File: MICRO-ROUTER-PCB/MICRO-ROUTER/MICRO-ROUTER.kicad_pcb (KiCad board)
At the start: 2 copper layers, 85 x 54 mm, 75 parts, among them J2 USB_A, J3 USB_C_Receptacle_USB2.0_16P, J4 Battery Connector, J5 SPI Header, J6 GPIO Header, J7 RJ45 5-2301996-6, Q1 FS8205A, SW2 8Devices Reset, SW3 UART Reset, U1 TP4056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

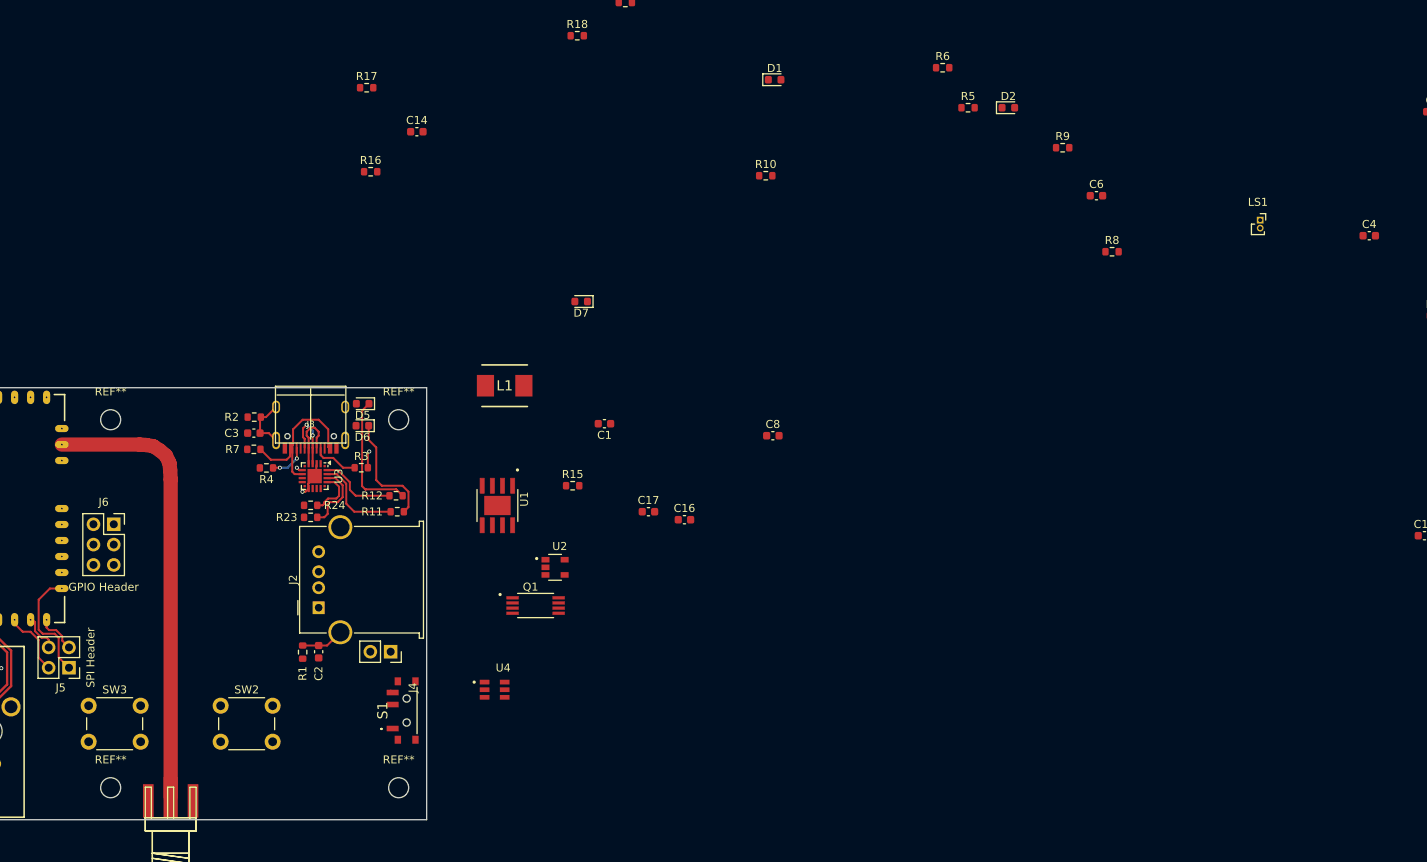
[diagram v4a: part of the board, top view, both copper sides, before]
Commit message: -added extra charge LED -wired TP4056
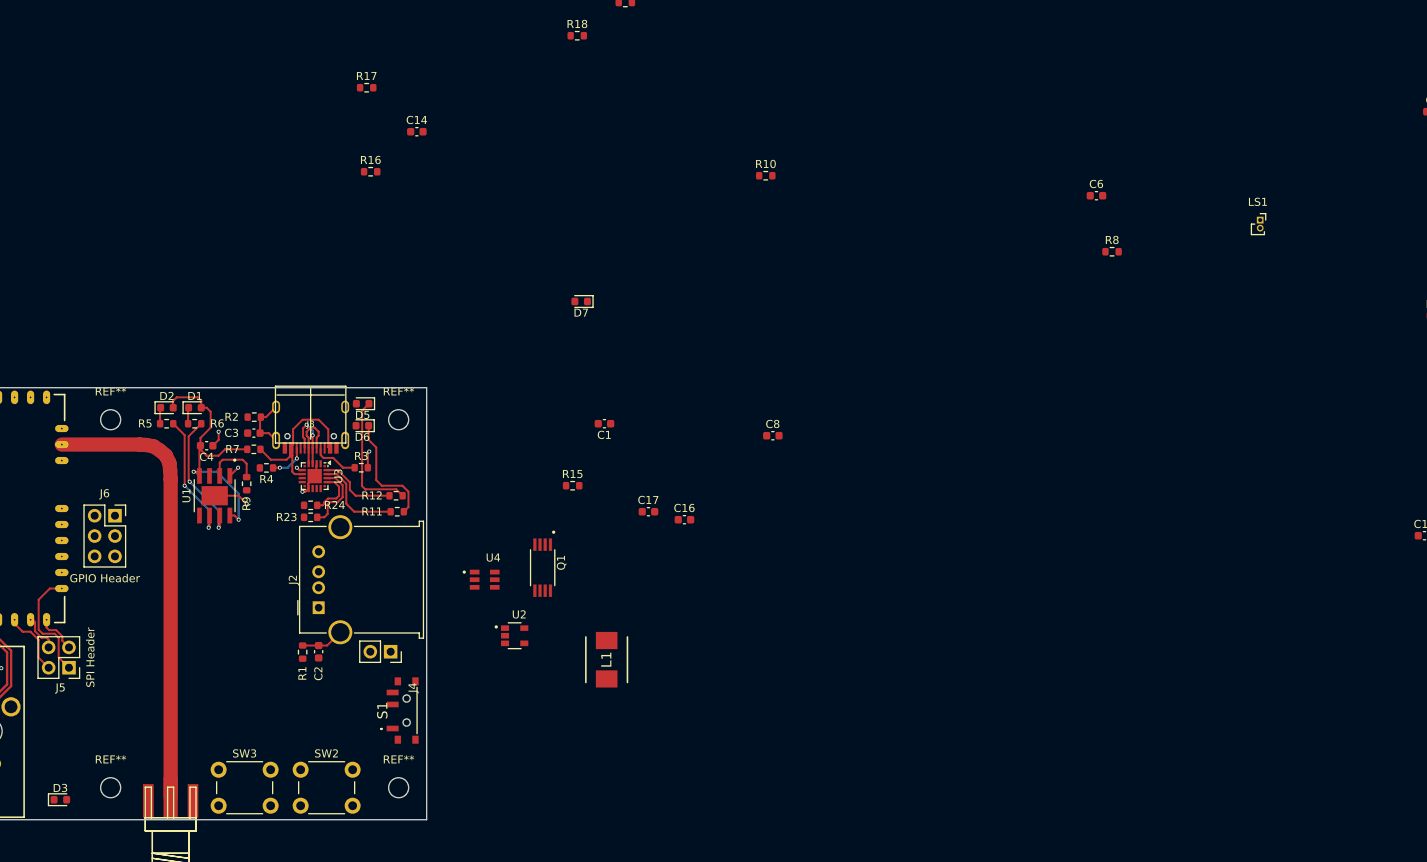
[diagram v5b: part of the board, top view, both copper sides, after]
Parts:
- added D3: LED Green, LED_SMD:LED_0603_1608Metric, F.Cu at (89.7, 184.5)
- moved C4 147.7 mm to (108.0, 140.2), turned to 180 degrees
- moved D2 111.7 mm to (103.0, 135.5)
- moved R9 110.3 mm to (113.0, 145.0), turned to -90 degrees
- moved R5 107.7 mm to (103.0, 137.5)
- moved R6 103.5 mm to (106.5, 137.5), turned to 180 degrees
- moved D1 83.3 mm to (106.5, 135.5)
- moved L1 36.5 mm to (158.0, 167.0), turned to 90 degrees
- moved U1 35.4 mm to (109.0, 146.5)
- moved SW3 18.1 mm to (109.5, 180.8)
- moved U4 13.8 mm to (142.8, 157.0)
- moved SW2 12.8 mm to (119.8, 180.8)
- moved U2 9.93 mm to (146.5, 164.0)
- moved Q1 4.81 mm to (150.0, 155.5), turned to -90 degrees
- moved J6 1.08 mm to (96.5, 149.0)
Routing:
- net Net-(D1-A): track 0.00 -> 34.9 mm, vias 0 -> 2
- net Net-(U1-~{CHRG}): track 0.00 -> 16.8 mm, vias 0 -> 2
- net Net-(U1-~{STDBY}): track 0.00 -> 16.4 mm, vias 0 -> 2
- net GND: track 6.55 -> 14.5 mm, vias 2 -> 5
- net Net-(U1-PROG): track 0.00 -> 7.06 mm
- net Net-(D2-K): track 0.00 -> 2.03 mm
- net Net-(D1-K): track 0.00 -> 2.03 mm
- net VBUS: track 20.1 -> 21.2 mm

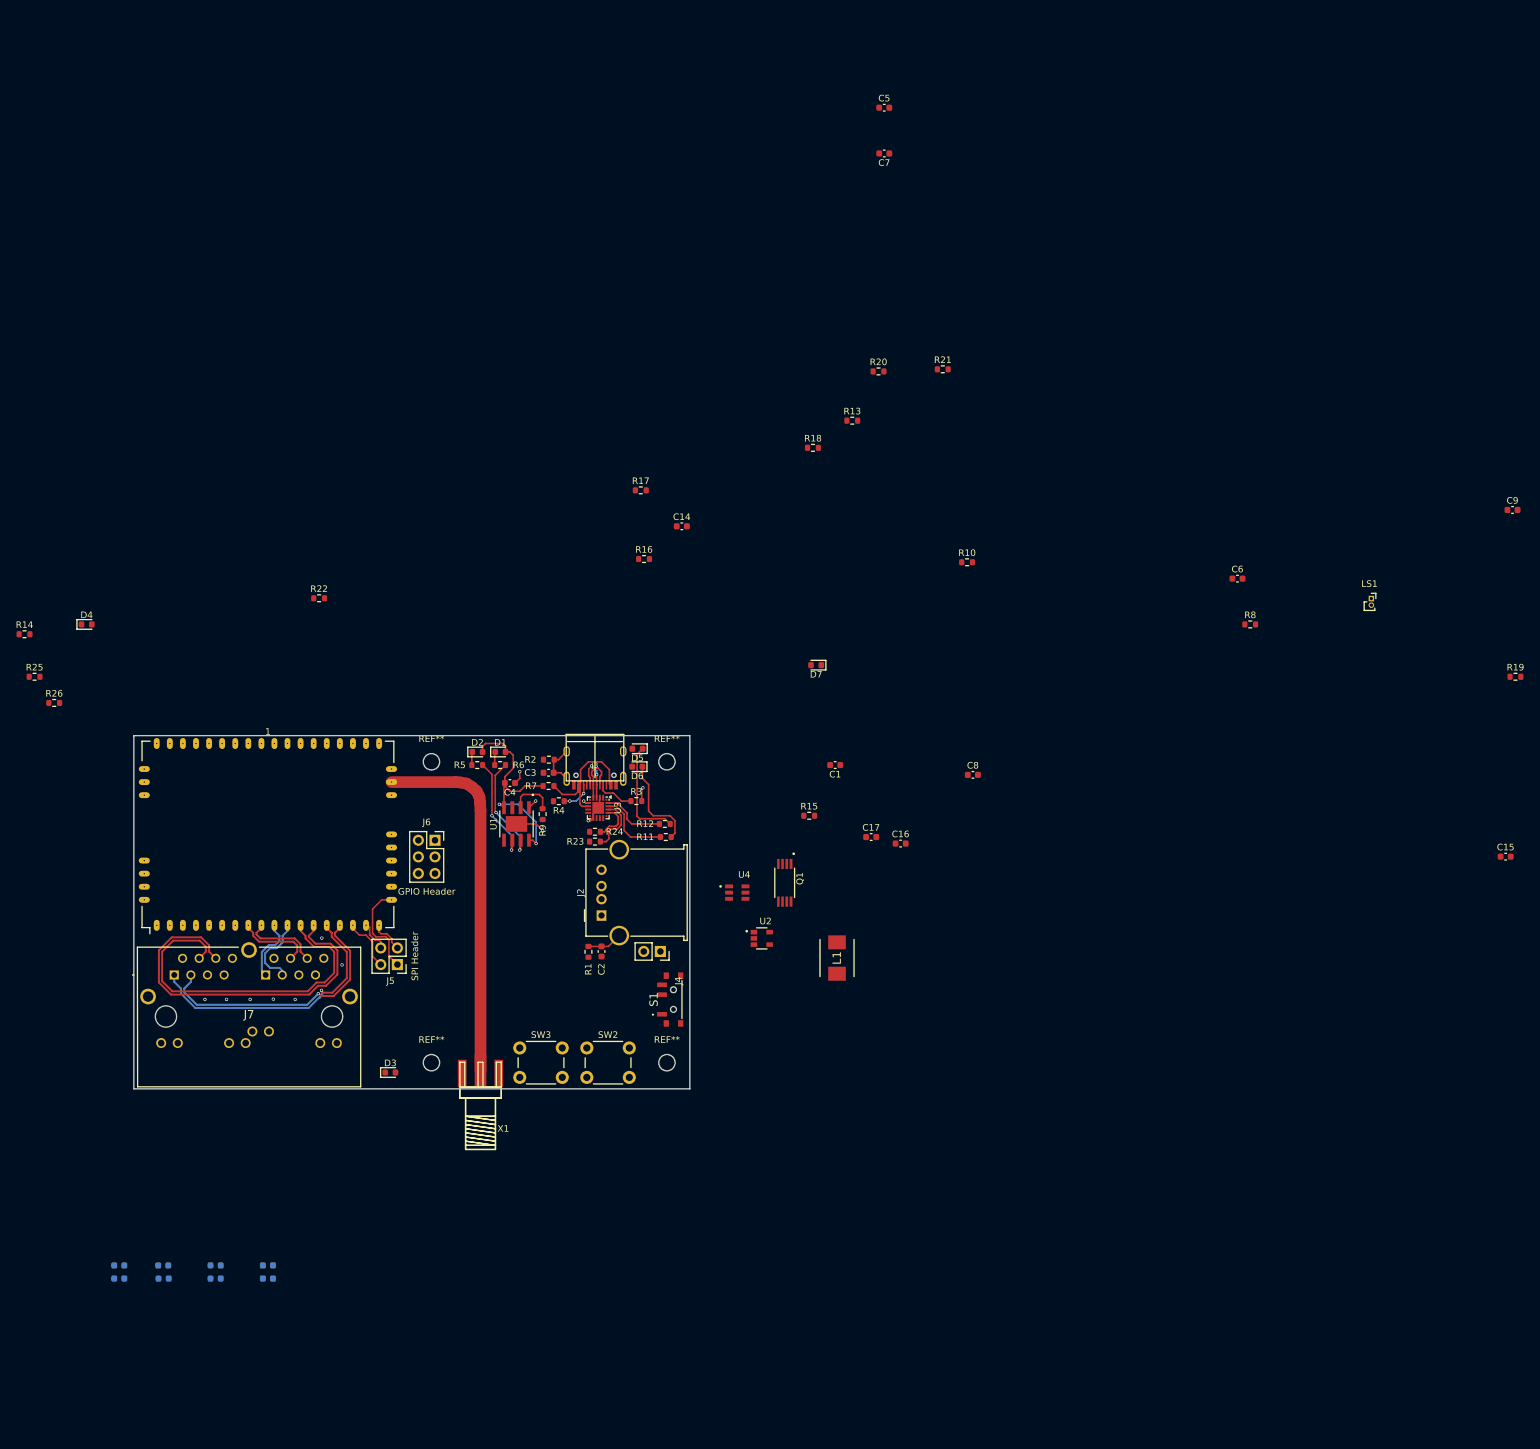
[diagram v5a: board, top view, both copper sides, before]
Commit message: -Wired up Mofset
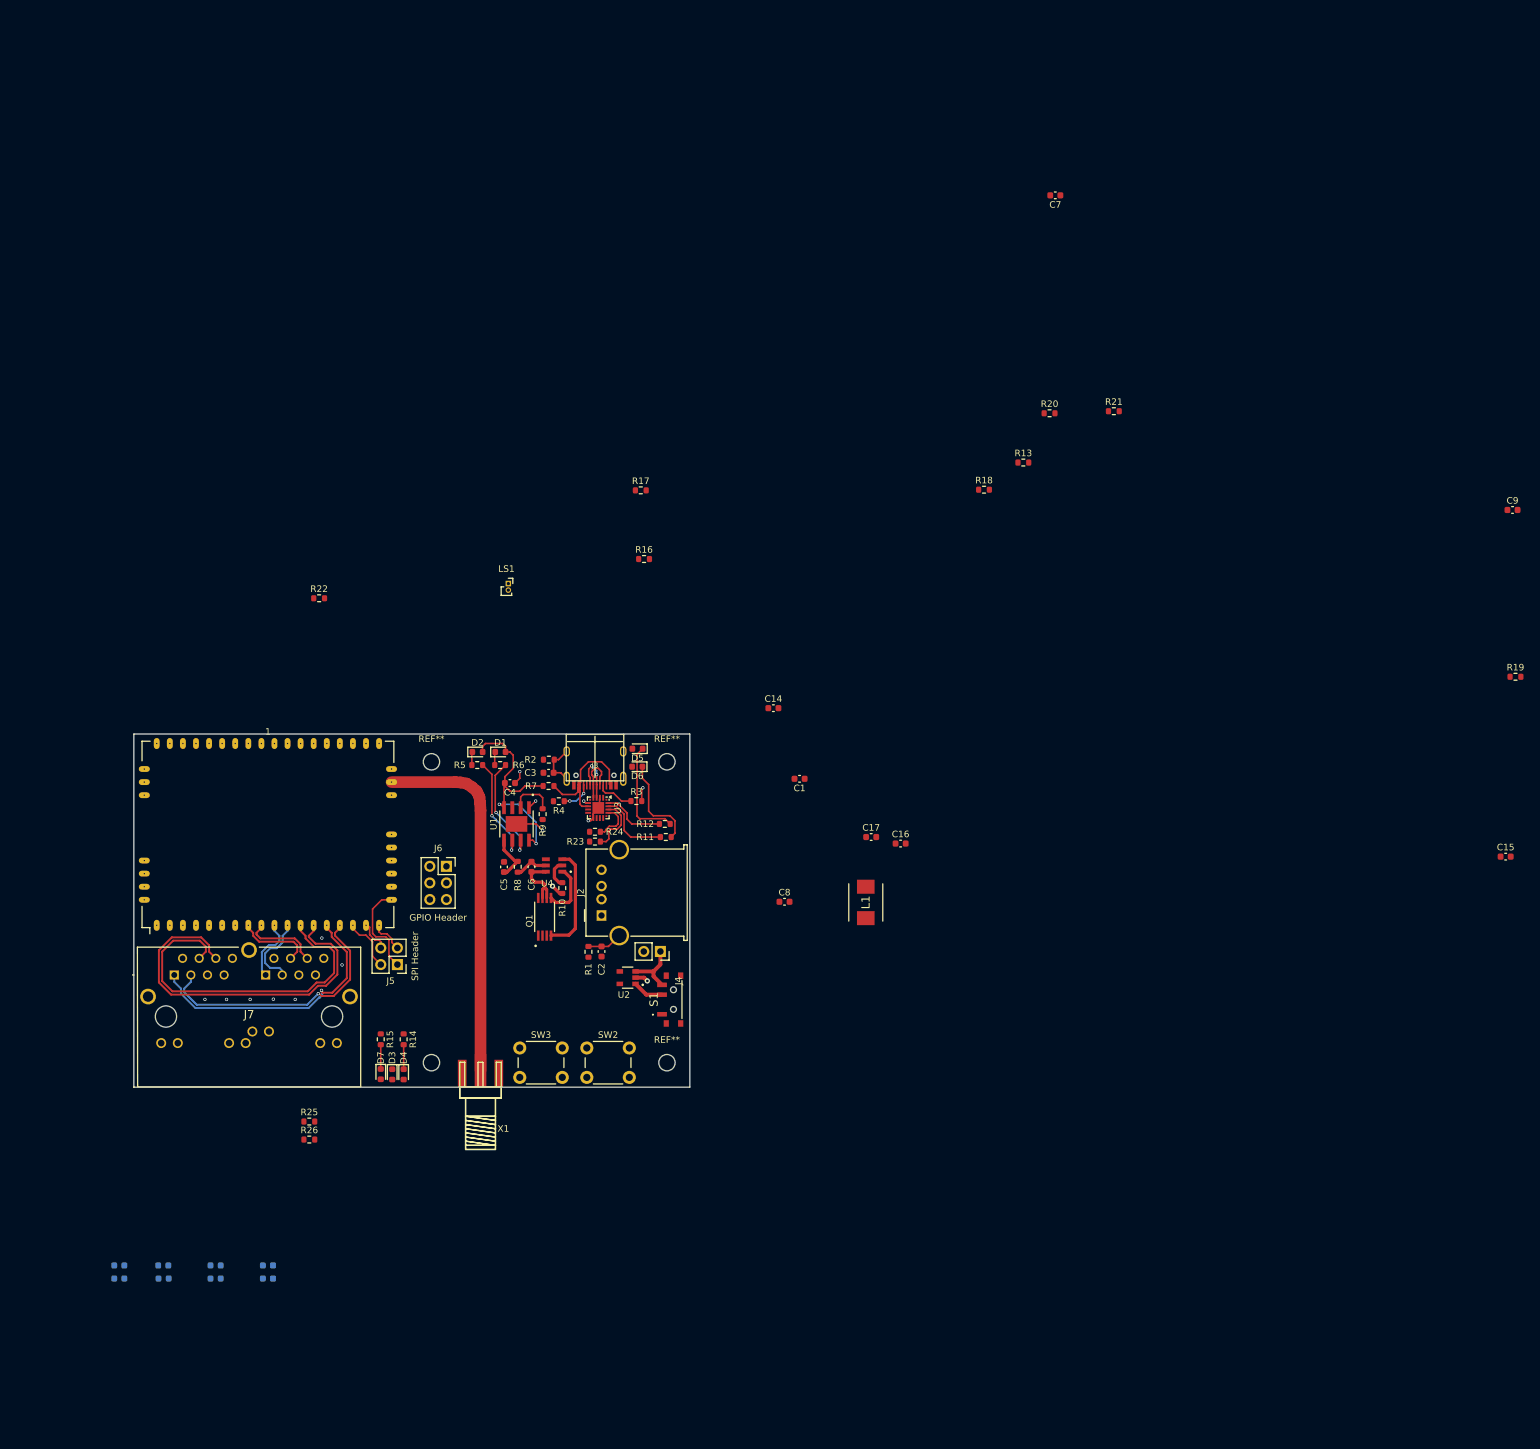
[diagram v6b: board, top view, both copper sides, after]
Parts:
- moved LS1 132.0 mm to (107.8, 109.8)
- moved C5 129.8 mm to (107.1, 153.1), turned to -90 degrees
- moved R8 118.0 mm to (109.2, 153.1), turned to -90 degrees
- moved C6 116.6 mm to (111.3, 153.1), turned to 90 degrees
- moved D7 91.3 mm to (88.2, 184.8), turned to -90 degrees
- moved R14 84.8 mm to (91.8, 179.4), turned to -90 degrees
- moved D4 84.1 mm to (91.8, 184.8), turned to -90 degrees
- moved R25 79.9 mm to (77.3, 192.0)
- moved R10 79.4 mm to (116.0, 156.3), turned to -90 degrees
- moved R26 77.3 mm to (77.3, 194.8)
- moved R15 73.9 mm to (88.2, 179.4), turned to -90 degrees
- moved Q1 37.1 mm to (113.3, 160.7), turned to 90 degrees
- moved C8 34.7 mm to (150.0, 158.4)
- moved C14 31.1 mm to (148.3, 128.8)
- moved U4 28.3 mm to (114.7, 152.8), turned to 180 degrees
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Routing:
- net Net-(U4-OC): track 0.00 -> 16.2 mm
- net V-UNREG: track 0.35 -> 15.9 mm
- net Net-(J4-Pin_2): track 0.00 -> 10.0 mm
- net Net-(U4-OD): track 0.00 -> 8.54 mm
- net Net-(U4-VCC): track 0.00 -> 5.20 mm
- net Net-(S1-COM): track 0.00 -> 4.73 mm
- net Net-(U4-CS): track 0.00 -> 4.28 mm
- net GND: track 14.5 -> 18.5 mm, vias 5 -> 7
- net Net-(D4-K): track 0.00 -> 3.75 mm
- net Net-(D7-K): track 0.00 -> 3.71 mm

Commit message: fixed reg
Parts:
- removed C9: 10uf, Capacitor_SMD:C_0603_1608Metric
- added L2: 4.7uf, Custom Footprints:INDPM5752X300N, F.Cu at (114.0, 168.8)
- added U5: XC9141A50DMR-G, Custom Footprints:XC8107AC20MR-G, F.Cu at (126.3, 170.4)
- moved C7 138.1 mm to (123.4, 170.6), turned to -90 degrees
- moved C15 80.7 mm to (181.8, 170.5)
- moved R19 80.7 mm to (183.3, 143.0)
- moved L1 51.1 mm to (114.0, 174.8), turned to 180 degrees
- moved C1 46.3 mm to (123.4, 175.8), turned to -90 degrees
- moved R13 45.0 mm to (148.8, 115.8)
- moved R18 45.0 mm to (142.8, 120.0)
- moved R20 45.0 mm to (152.8, 108.3)
- moved R21 45.0 mm to (162.6, 108.0)
- moved LS1 38.7 mm to (98.2, 147.2), turned to 90 degrees
- moved C17 28.6 mm to (157.3, 176.5)
- moved C8 18.0 mm to (133.8, 166.2), turned to 90 degrees
- moved U2 5.56 mm to (126.3, 175.6)
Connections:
- net Net-(S1-COM) renamed V-UNREG SW
- C7 pad 1: V-UNREG -> +5V
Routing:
- net V-UNREG: track 15.9 -> 91.6 mm
- net Net-(U2-LX): track 0.00 -> 12.6 mm
- net Net-(U5-LX): track 0.00 -> 12.2 mm
- net V-UNREG SW: track 4.73 -> 9.74 mm
- net GND: track 18.5 -> 23.5 mm, vias 7 -> 9
- net +3.3V: track 0.80 -> 2.68 mm
- net +5V: track 0.00 -> 1.84 mm
- net (no net): vias 7 -> 8
